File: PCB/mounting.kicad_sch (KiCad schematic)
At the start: 26 parts

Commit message: Update and pre-production output
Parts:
- removed H11, H21, H6: MountingHole, cipulot_parts:HOLE_M2_RF, symbol Mechanical:MountingHole
- added H10, H13, H19, H22, H24, H27, H28, H29, H31, H32, H33, H35, H36, H37, H39, H4, H40, H41, H43, H44, H45, H7: MountingHole, cipulot_parts:HOLE_M2_RF, symbol Mechanical:MountingHole
- renumbered H7 to H11, H10 to H16, H13 to H21, H16 to H26, H19 to H30, H22 to H34, H24 to H38, H26 to H42, H4 to H6
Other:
- moved on the sheet: H1, H11, H16, H21, H26, H30, H34, H38, H42, H6

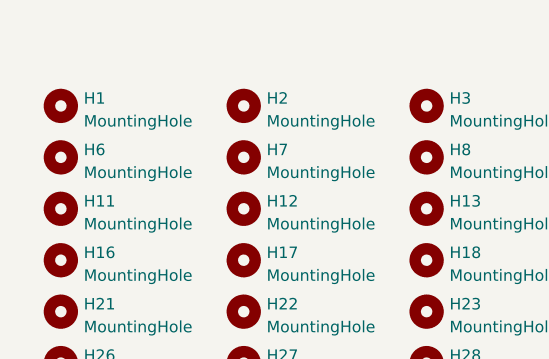
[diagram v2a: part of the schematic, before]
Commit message: Update of PCB
Added shielding copper pad for plate electrical connection, along with EMI filtering through capacitor and inductor.
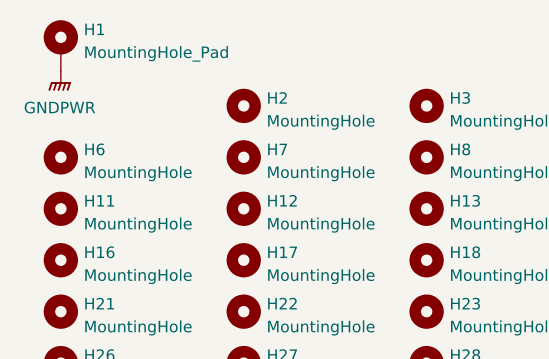
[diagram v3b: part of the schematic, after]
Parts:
- removed H1: MountingHole, cipulot_parts:HOLE_M2_RF, symbol Mechanical:MountingHole
- added H1: MountingHole_Pad, cipulot_parts:M2.5_RF_Shield, symbol Mechanical:MountingHole_Pad
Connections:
- new net GNDPWR: H1.1
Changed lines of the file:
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@@
     )
+  )
+  (symbol (lib_id "Mechanical:MountingHole_Pad") (at 52.07 33.02 0) (unit 1)
+    (in_bom yes) (on_board yes) (fields_autoplaced)
+    (property "Reference" "H1" (id 0) (at 54.61 30.9153 0)
+      (effects (font (size 1.27 1.27)) (justify left))
+    )
+    (property "Value" "MountingHole_Pad" (id 1) (at 54.61 33.4522 0)
+      (effects (font (size 1.27 1.27)) (justify left))
+    )
+    (property "Footprint" "cipulot_parts:M2.5_RF_Shield" (id 2) (at 52.07 33.02 0)
+      (effects (font (size 1.27 1.27)) hide)
+    )
+    (property "Datasheet" "~" (id 3) (at 52.07 33.02 0)
+      (effects (font (size 1.27 1.27)) hide)
+    )
+    (pin "1")
   )
   (symbol (lib_id "Mechanical:MountingHole") (at 52.07 85.09 0) (unit 1)
@@
     )
   )
+  (symbol (lib_id "power:GNDPWR") (at 52.07 35.56 0) (unit 1)
+    (in_bom yes) (on_board yes) (fields_autoplaced)
+    (property "Reference" "#PWR067" (id 0) (at 52.07 40.64 0)
+      (effects (font (size 1.27 1.27)) hide)
+    )
+    (property "Value" "GNDPWR" (id 1) (at 51.943 39.597 0))
+    (property "Footprint" "" (id 2) (at 52.07 36.83 0)
+      (effects (font (size 1.27 1.27)) hide)
+    )
+    (property "Datasheet" "" (id 3) (at 52.07 36.83 0)
+      (effects (font (size 1.27 1.27)) hide)
+    )
+    (pin "1")
+  )
   (symbol (lib_id "Mechanical:MountingHole") (at 113.03 45.085 0) (unit 1)
     (in_bom yes) (on_board yes) (fields_autoplaced)
@@
       (effects (font (size 1.27 1.27)) hide)
     )
-  )
-  (symbol (lib_id "Mechanical:MountingHole") (at 52.07 39.37 0) (unit 1)
-    (in_bom yes) (on_board yes) (fields_autoplaced)
-    (property "Reference" "H1" (id 0) (at 54.61 38.5353 0)
-      (effects (font (size 1.27 1.27)) (justify left))
-    )
-    (property "Value" "MountingHole" (id 1) (at 54.61 41.0722 0)
-      (effects (font (size 1.27 1.27)) (justify left))
-    )
-    (property "Footprint" "cipulot_parts:HOLE_M2_RF" (id 2) (at 52.07 39.37 0)
-      (effects (font (size 1.27 1.27)) hide)
-    )
-    (property "Datasheet" "~" (id 3) (at 52.07 39.37 0)
-      (effects (font (size 1.27 1.27)) hide)
-    )

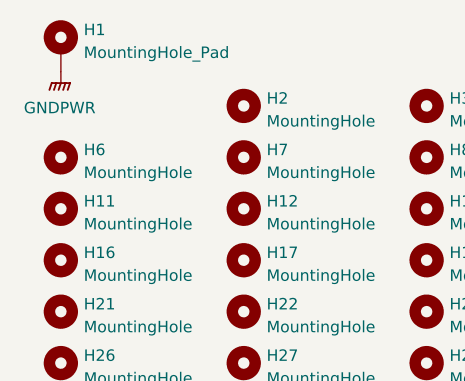
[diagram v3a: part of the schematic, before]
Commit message: Updated files for Rev 1.1
Features added:
- THT LED for Caps Lock and Scroll Lock
- moved filtering components for plate shield to top side
- added filtering components for USB-C shield

Firmware updated accordingly too.
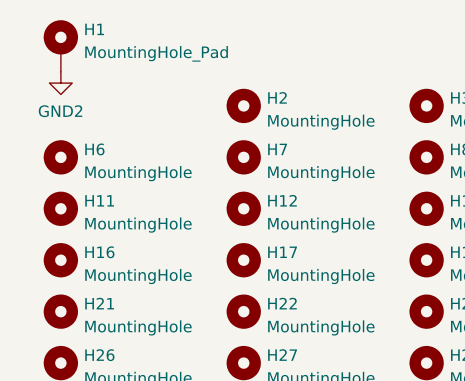
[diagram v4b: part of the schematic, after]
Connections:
- net GNDPWR renamed GND2
